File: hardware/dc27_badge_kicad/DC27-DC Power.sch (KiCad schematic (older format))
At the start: 22 parts, among them SW401 POWER ON, U401 MCP73833, U402 LM1117-3.3

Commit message: PROTOV2 OFF TO MACROFAB
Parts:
- C406: footprint Capacitor_SMD:C_0603_1608Metric -> Capacitor_SMD:C_1206_3216Metric
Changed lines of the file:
@@
 F 0 "C406" H 5100 3850 50  0000 L CNN
 F 1 "10uF" H 5100 3750 50  0000 L CNN
-F 2 "Capacitor_SMD:C_0603_1608Metric" H 5038 3550 50  0001 C CNN
+F 2 "Capacitor_SMD:C_1206_3216Metric" H 5038 3550 50  0001 C CNN
 F 3 "~" H 5000 3700 50  0001 C CNN
 	1    5000 3700

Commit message: check in charging circuit changes
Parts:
- added D404: SD0603S040S0R2, Diode_SMD:D_0603_1608Metric, symbol DC27-badge-rescue:D_Schottky-Device
- added Q401: FDN360P, Package_TO_SOT_SMD:SOT-23, symbol Transistor_FET:Si2319CDS
- added R407: 10K, Resistor_SMD:R_0603_1608Metric, symbol Device:R
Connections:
- net GND: now also R407.2
- net VBUS: now also D404.2 (A), Q401.1 (G), R407.1
- net at BT401.1 (+), C406.1, TP401.1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: now also Q401.3 (D); no longer SW401.3 (C)
- new net: D404.1 (K), Q401.2 (S), SW401.3 (C)
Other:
- moved on the sheet: C401, C402, C403, C404, SW401, TP402, TP403, U402

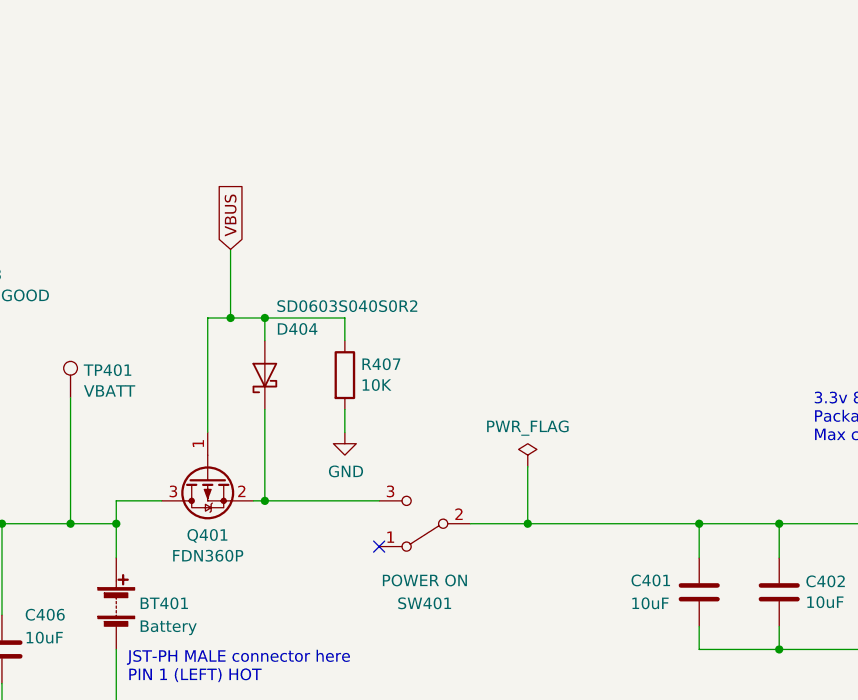
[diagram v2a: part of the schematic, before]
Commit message: add test points for the DAC. Add new context secret codes
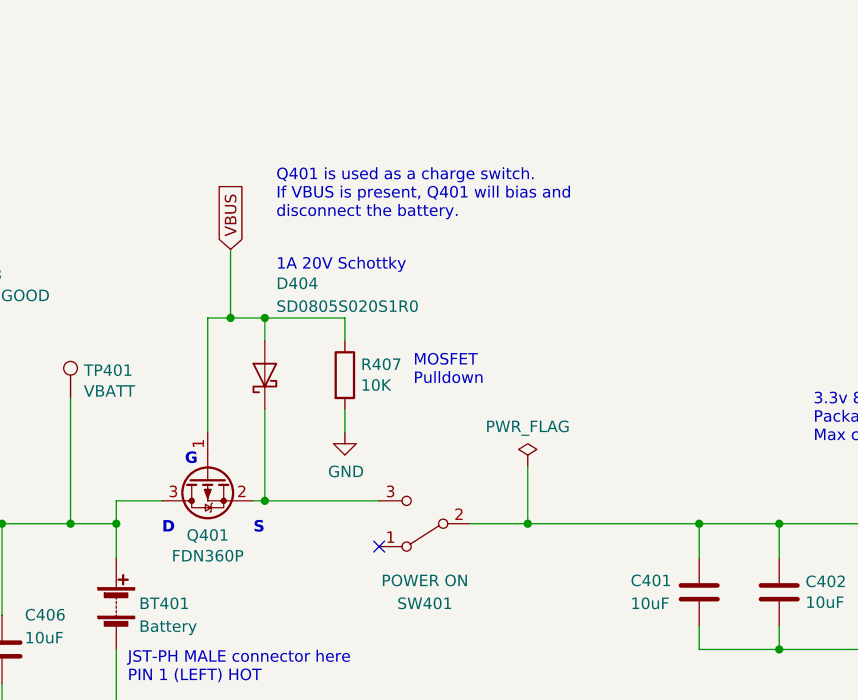
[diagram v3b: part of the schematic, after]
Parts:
- D404: value SD0603S040S0R2 -> SD0805S020S1R0; footprint Diode_SMD:D_0603_1608Metric -> Diode_SMD:D_0805_2012Metric
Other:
- note added: "1A 20V Schottky\n"
- note added: "D"
- note added: "G"
- note added: "MOSFET\nPulldown"
- note added: "Q401 is used as a charge switch. \nIf VBUS is present, Q401 will bias and\ndisconnect the battery.\n\n"
- note added: "S"
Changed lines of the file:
@@
 U 1 1 5CE7938B
 P 6150 2500
-F 0 "D404" V 6350 2450 50  0000 R CNN
-F 1 "SD0603S040S0R2" V 6450 2450 50  0000 R CNN
-F 2 "Diode_SMD:D_0603_1608Metric" H 6150 2500 50  0001 C CNN
+F 0 "D404" V 6550 2450 50  0000 R CNN
+F 1 "SD0805S020S1R0" V 6450 2450 50  0000 R CNN
+F 2 "Diode_SMD:D_0805_2012Metric" H 6150 2500 50  0001 C CNN
 F 3 "" H 6150 2500 50  0001 C CNN
 	1    6150 2500
@@
 	6500 2250 6150 2250
 Connection ~ 6150 2250
+Text Notes 6200 2050 0    50   ~ 0
+1A 20V Schottky\n
+Text Notes 6800 2550 0    50   ~ 0
+MOSFET\nPulldown
+Text Notes 6200 1900 0    50   ~ 0
+Q401 is used as a charge switch. \nIf VBUS is present, Q401 will bias and\ndisconnect the battery.\n\n
+Text Notes 6100 3200 0    50   ~ 10
+S
+Text Notes 5700 3200 0    50   ~ 10
+D
+Text Notes 5800 2900 0    50   ~ 10
+G
 $EndSCHEMATC

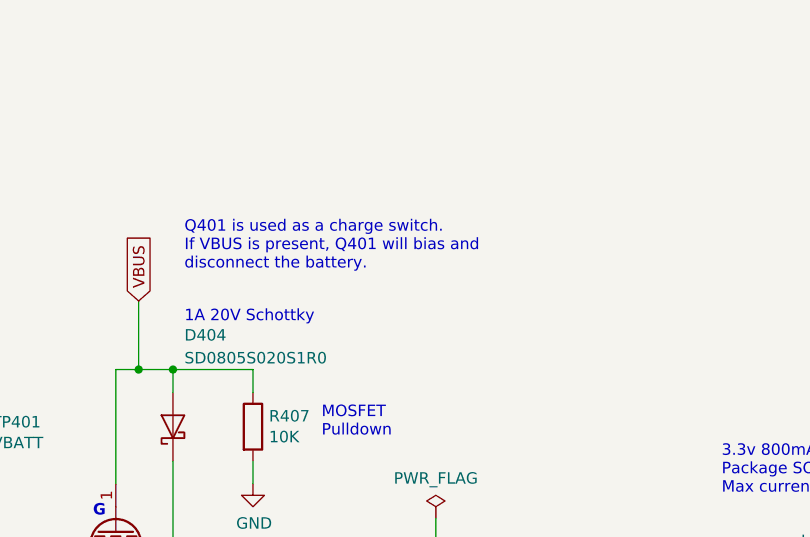
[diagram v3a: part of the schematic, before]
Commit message: move config reset to both selects held down, add meteor_red led pattern, fix the unlock screen
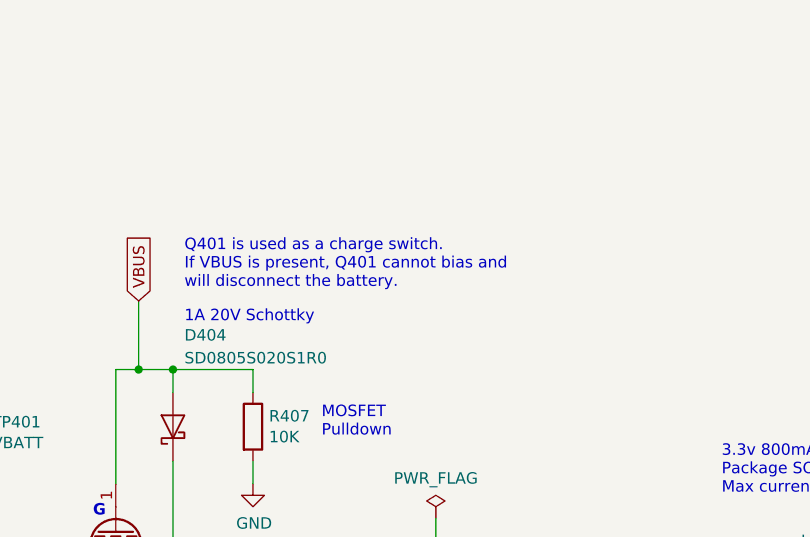
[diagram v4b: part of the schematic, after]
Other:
- note added: "Q401 is used as a charge switch. \nIf VBUS is present, Q401 cannot bias and\nwill disconnect the battery."
- note removed: "Q401 is used as a charge switch. \nIf VBUS is present, Q401 will bias and\ndisconnect the battery.\n\n"
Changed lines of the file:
@@
 MOSFET\nPulldown
 Text Notes 6200 1900 0    50   ~ 0
-Q401 is used as a charge switch. \nIf VBUS is present, Q401 will bias and\ndisconnect the battery.\n\n
+Q401 is used as a charge switch. \nIf VBUS is present, Q401 cannot bias and\nwill disconnect the battery.
 Text Notes 6100 3200 0    50   ~ 10
 S
